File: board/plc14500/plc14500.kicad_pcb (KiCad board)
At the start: 2 copper layers, 160.1 x 99.9 mm, 167 parts, among them U1 74HC14, U10 MC14500, U11 74HC14, U12 4011, U13 4099, U14 4051, U2 4051, U3 74HC14, U4 NE555, U5 4099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

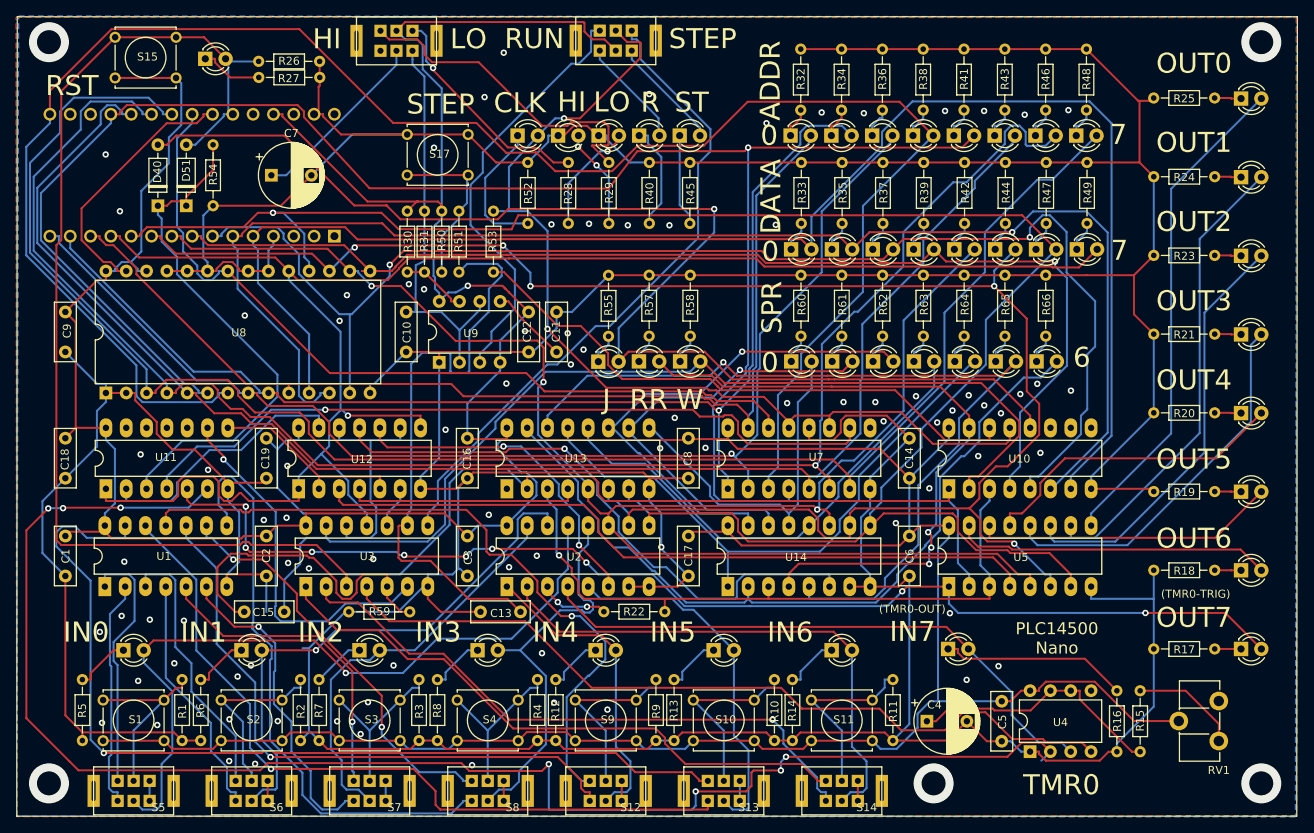
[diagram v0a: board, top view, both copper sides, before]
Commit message: Rearrange LEDs
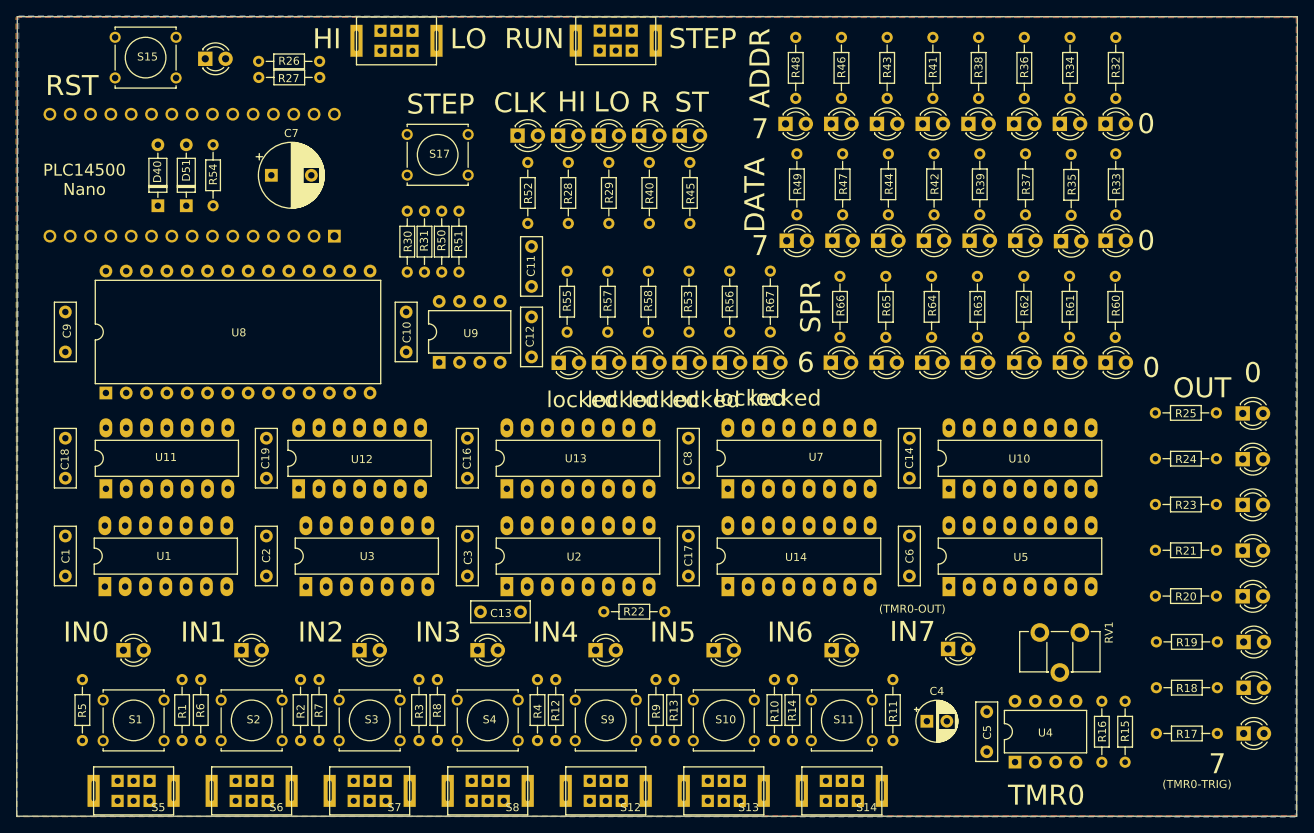
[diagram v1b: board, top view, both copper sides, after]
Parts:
- removed C15: 100nF, Capacitor_THT:C_Rect_L7.2mm_W2.5mm_P5.00mm_FKS2_FKP2_MKS2_MKP2
- removed R59: 3K3, Resistor_THT:R_Axial_DIN0204_L3.6mm_D1.6mm_P7.62mm_Horizontal
- added D50: LED 3MM Red, plc14500:LED_3MM, F.Cu at (154.4, 86.4)
- added D52: LED 3MM Red, plc14500:LED_3MM, F.Cu at (159.4, 86.4)
- added D53: LED 3MM Red, plc14500:LED_3MM, F.Cu at (164.5, 86.4)
- added R56: 820R, Resistor_THT:R_Axial_DIN0204_L3.6mm_D1.6mm_P7.62mm_Horizontal, F.Cu at (160.7, 82.5)
- added R67: 820R, Resistor_THT:R_Axial_DIN0204_L3.6mm_D1.6mm_P7.62mm_Horizontal, F.Cu at (165.7, 74.9)
- C4: value 470uF -> 10uF; footprint Capacitor_THT:CP_Radial_D8.0mm_P5.00mm -> Capacitor_THT:CP_Radial_D5.0mm_P2.50mm
- RV1: value 10K -> 1M
- moved D20 39.4 mm to (207.6, 56.5)
- moved R32 39.4 mm to (208.9, 45.7)
- moved R25 39.4 mm to (213.9, 92.6)
- moved D16 39.4 mm to (224.8, 92.7)
- moved D21 39.3 mm to (207.6, 71.1)
- moved R33 39.3 mm to (208.9, 60.3)
- moved R60 39.3 mm to (208.9, 75.6)
- moved D43 39.3 mm to (207.6, 86.4)
- moved D36 36.4 mm to (167.6, 56.5)
- moved R48 36.4 mm to (168.9, 45.7)
- moved D37 36.3 mm to (167.8, 71.1)
- moved R49 36.3 mm to (169.1, 60.3)
- moved D15 35.2 mm to (224.8, 98.4)
- moved R24 35.2 mm to (213.9, 98.4)
- moved D14 31.1 mm to (224.8, 104.1)
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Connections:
- D38 pad A: CLK -> /CPU/CLK2
- R53 pad 1: Net-(R53-Pad1) -> GND
- R53 pad 2: CLK -> Net-(D50-C)
- RV1 pad 3: (no net) -> unconnected-(RV1-Pad3)
- S16 pad 7: (no net) -> unconnected-(S16-Pad7)
- S18 pad 2: CLK -> /CPU/CLK2
- U10 pad 10: (no net) -> Net-(U10-FLAG0)
- U10 pad 11: (no net) -> Net-(U10-RTN)
- U10 pad 13: CLK -> /CPU/CLK2
- U10 pad 14: Net-(R53-Pad1) -> /CPU/CLK1
- U10 pad 9: (no net) -> Net-(U10-FLAGF)
- U11 pad 8: Net-(U11-Pad8) -> (no net)
- U11 pad 9: Net-(U11-Pad9) -> (no net)
- U12 pad 2: Net-(U11-Pad8) -> W
- U12 pad 5: Net-(U11-Pad8) -> W
- U13 pad 1: (no net) -> unconnected-(U13-Q7-Pad1)
- U3 pad 5: Net-(C15-Pad1) -> (no net)
- U3 pad 6: Net-(U11-Pad9) -> (no net)
- U4 pad 5: (no net) -> unconnected-(U4-CON-Pad5)
- U6 pad 1: (no net) -> unconnected-(U6-D1/TX-Pad1)
- U6 pad 17: (no net) -> unconnected-(U6-3V3-Pad17)
- U6 pad 18: (no net) -> unconnected-(U6-AREF-Pad18)
- U6 pad 2: (no net) -> unconnected-(U6-D0/RX-Pad2)
- U6 pad 26: (no net) -> unconnected-(U6-A7-Pad26)
- U6 pad 28: (no net) -> unconnected-(U6-~{RESET}-Pad28)
- U6 pad 3: (no net) -> unconnected-(U6-~{RESET}-Pad3)
- U6 pad 30: (no net) -> unconnected-(U6-VIN-Pad30)
- U7 pad 11: CLK -> /CPU/CLK1
- U7 pad 13: CLK -> /CPU/CLK1
- U7 pad 9: (no net) -> unconnected-(U7-~{RCO}-Pad9)
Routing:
- net GND: track 854.5 -> 0.00 mm, vias 92 -> 0
- net +5V: track 586.3 -> 0.00 mm, vias 1 -> 0
- net D6: track 244.9 -> 0.00 mm, vias 1 -> 0
- net RES: track 243.9 -> 0.00 mm
- net A3: track 236.5 -> 0.00 mm
- net D5: track 224.5 -> 0.00 mm, vias 5 -> 0
- net A4: track 221.3 -> 0.00 mm, vias 1 -> 0
- net D7: track 216.0 -> 0.00 mm, vias 1 -> 0
- net A7: track 213.1 -> 0.00 mm
- net D4: track 207.6 -> 0.00 mm, vias 3 -> 0
- net A6: track 206.9 -> 0.00 mm, vias 1 -> 0
- net Net-(U4-TRI): track 194.0 -> 0.00 mm, vias 7 -> 0
- net D0: track 191.5 -> 0.00 mm
- net A5: track 190.1 -> 0.00 mm
- net D1: track 177.8 -> 0.00 mm, vias 1 -> 0
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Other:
- board text added: "OUT"
- board text added: "REV.D"
- board text added: "locked"
- board text removed: "J"
- board text removed: "OUT0"
- board text removed: "OUT1"
- board text removed: "OUT2"
- board text removed: "OUT3"
- board text removed: "OUT4"
- board text removed: "OUT5"
- board text removed: "OUT6"
- board text removed: "OUT7"
- board text removed: "RR"
- board text removed: "W"

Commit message: REV.D Schema updates
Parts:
- moved R51 1.45 mm to (128.3, 75.0)
- moved R50 1.06 mm to (125.7, 75.0)
- moved R31 0.68 mm to (123.2, 75.0)
- moved R30 0.30 mm to (120.7, 75.0)
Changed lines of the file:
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@@
   )
   (footprint "Resistor_THT:R_Axial_DIN0204_L3.6mm_D1.6mm_P7.62mm_Horizontal" locked (layer "F.Cu")
-    (at 120.355 75.04 90)
+    (at 120.65 75.04 90)
     (descr "Resistor, Axial_DIN0204 series, Axial, Horizontal, pin pitch=7.62mm, 0.167W, length*diameter=3.6*1.6mm^2, http://cdn-reichelt.de/documents/datenblatt/B400/1_4W%23YAG.pdf")
     (tags "Resistor Axial_DIN0204 series Axial Horizontal pin pitch 7.62mm 0.167W length 3.6mm diameter 1.6mm")
@@
   )
   (footprint "Resistor_THT:R_Axial_DIN0204_L3.6mm_D1.6mm_P7.62mm_Horizontal" locked (layer "F.Cu")
-    (at 122.51 75.04 90)
+    (at 123.19 75.04 90)
     (descr "Resistor, Axial_DIN0204 series, Axial, Horizontal, pin pitch=7.62mm, 0.167W, length*diameter=3.6*1.6mm^2, http://cdn-reichelt.de/documents/datenblatt/B400/1_4W%23YAG.pdf")
     (tags "Resistor Axial_DIN0204 series Axial Horizontal pin pitch 7.62mm 0.167W length 3.6mm diameter 1.6mm")
@@
   )
   (footprint "Resistor_THT:R_Axial_DIN0204_L3.6mm_D1.6mm_P7.62mm_Horizontal" locked (layer "F.Cu")
-    (at 124.665 75.04 90)
+    (at 125.73 75.04 90)
     (descr "Resistor, Axial_DIN0204 series, Axial, Horizontal, pin pitch=7.62mm, 0.167W, length*diameter=3.6*1.6mm^2, http://cdn-reichelt.de/documents/datenblatt/B400/1_4W%23YAG.pdf")
     (tags "Resistor Axial_DIN0204 series Axial Horizontal pin pitch 7.62mm 0.167W length 3.6mm diameter 1.6mm")
@@
   )
   (footprint "Resistor_THT:R_Axial_DIN0204_L3.6mm_D1.6mm_P7.62mm_Horizontal" locked (layer "F.Cu")
-    (at 126.82 75.04 90)
+    (at 128.27 75.04 90)
     (descr "Resistor, Axial_DIN0204 series, Axial, Horizontal, pin pitch=7.62mm, 0.167W, length*diameter=3.6*1.6mm^2, http://cdn-reichelt.de/documents/datenblatt/B400/1_4W%23YAG.pdf")
     (tags "Resistor Axial_DIN0204 series Axial Horizontal pin pitch 7.62mm 0.167W length 3.6mm diameter 1.6mm")
@@
     (effects (font (size 2.5 2.5) (thickness 0.6)))
   )
-  (gr_text "LO" (at 128.01 45.905) (layer "F.SilkS")
+  (gr_text "LO" (at 110.49 45.72) (layer "F.SilkS")
     (effects (font (size 2.5 2.5) (thickness 0.6)))
   )
-  (gr_text "HI" (at 110.32 45.905) (layer "F.SilkS")
+  (gr_text "HI" (at 126.365 45.905) (layer "F.SilkS")
     (effects (font (size 2.5 2.5) (thickness 0.6)))
   )
-  (gr_text "RUN" (at 136.24 45.885) (layer "F.SilkS")
+  (gr_text "RUN" (at 156.21 45.72) (layer "F.SilkS")
     (effects (font (size 2.5 2.5) (thickness 0.6)))
   )
-  (gr_text "STEP" (at 157.29 45.885) (layer "F.SilkS")
+  (gr_text "STEP" (at 135.89 45.885) (layer "F.SilkS")
     (effects (font (size 2.5 2.5) (thickness 0.6)))
   )
